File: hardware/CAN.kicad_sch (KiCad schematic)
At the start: 7 parts, among them U4 MCP2542FDxMF

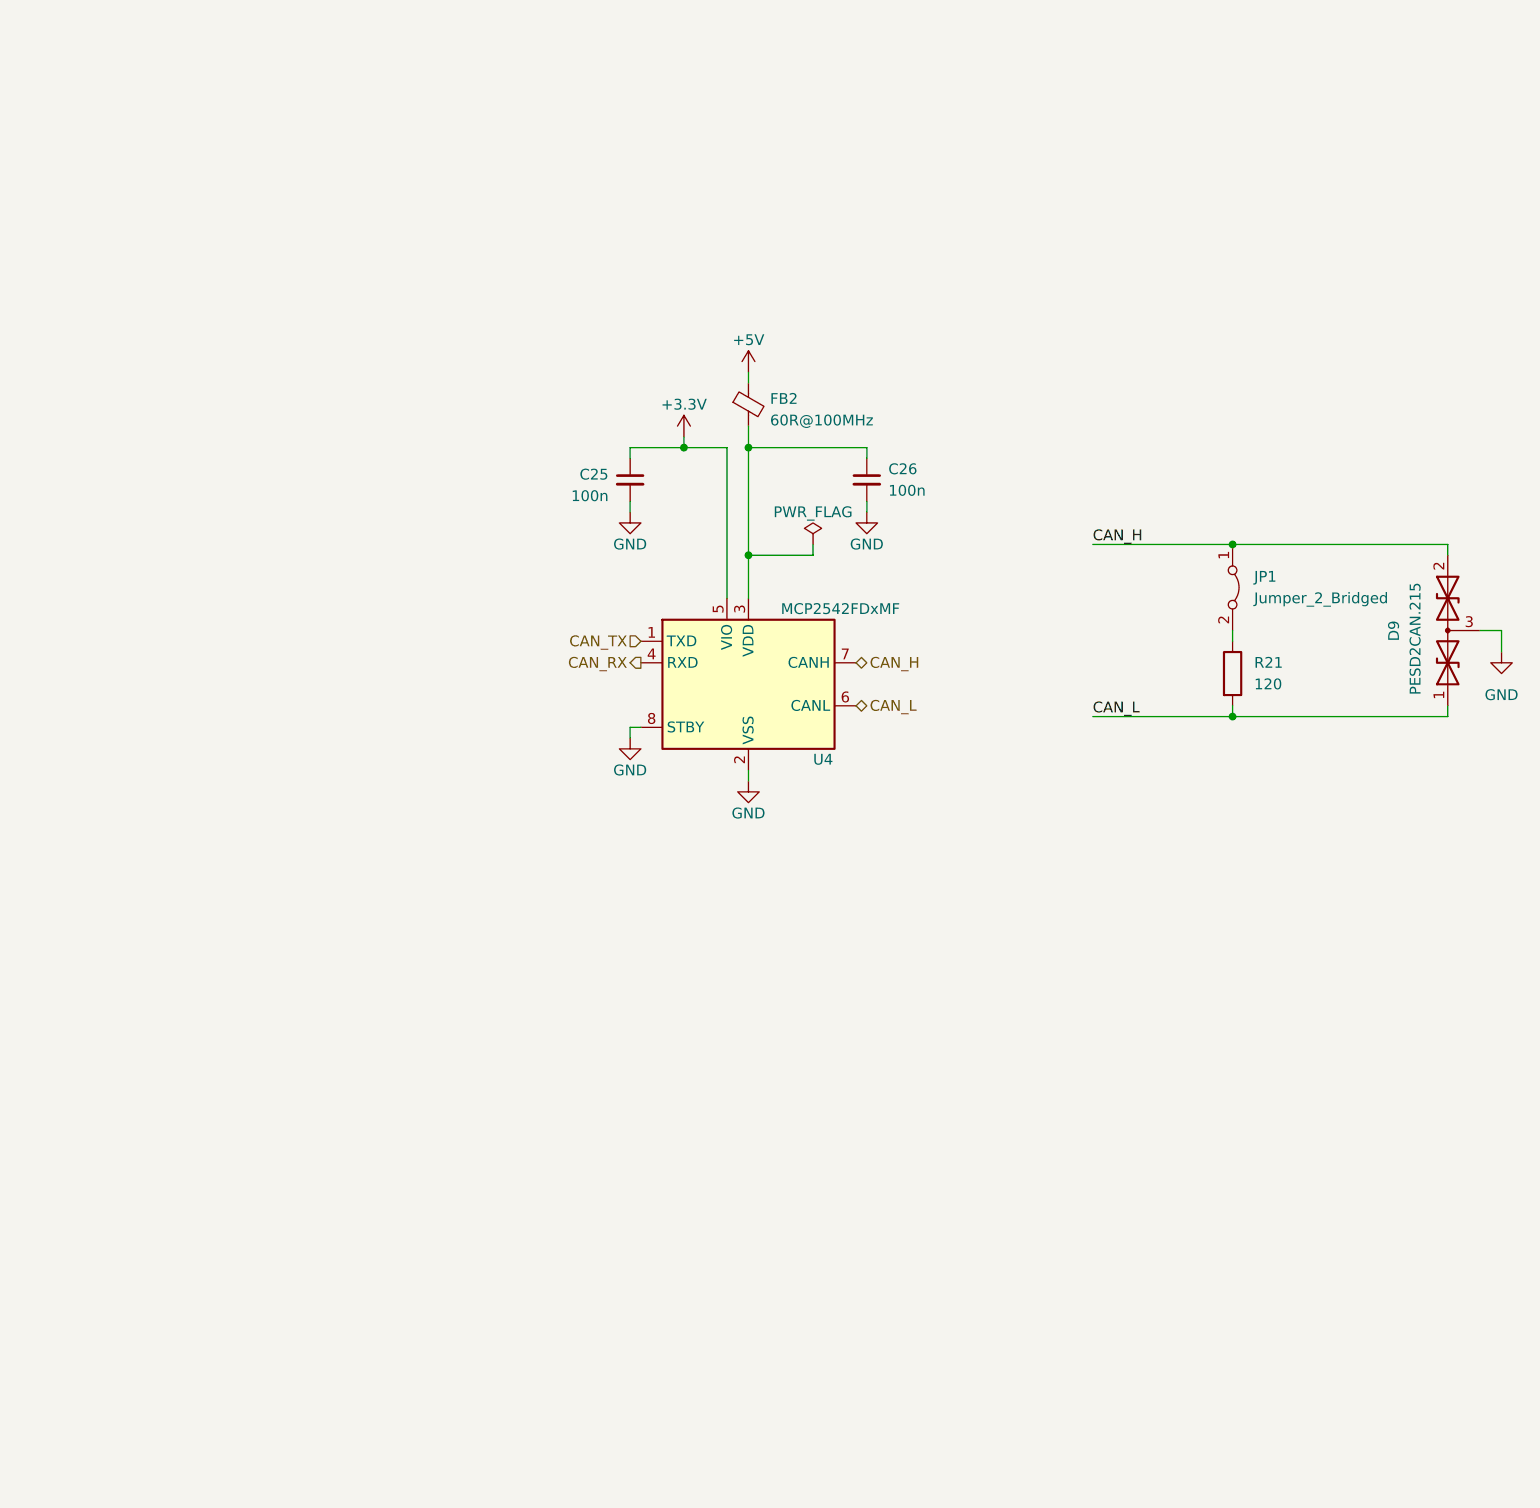
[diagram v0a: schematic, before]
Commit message: Changed CAN to isolated and added a new board-to-board plug
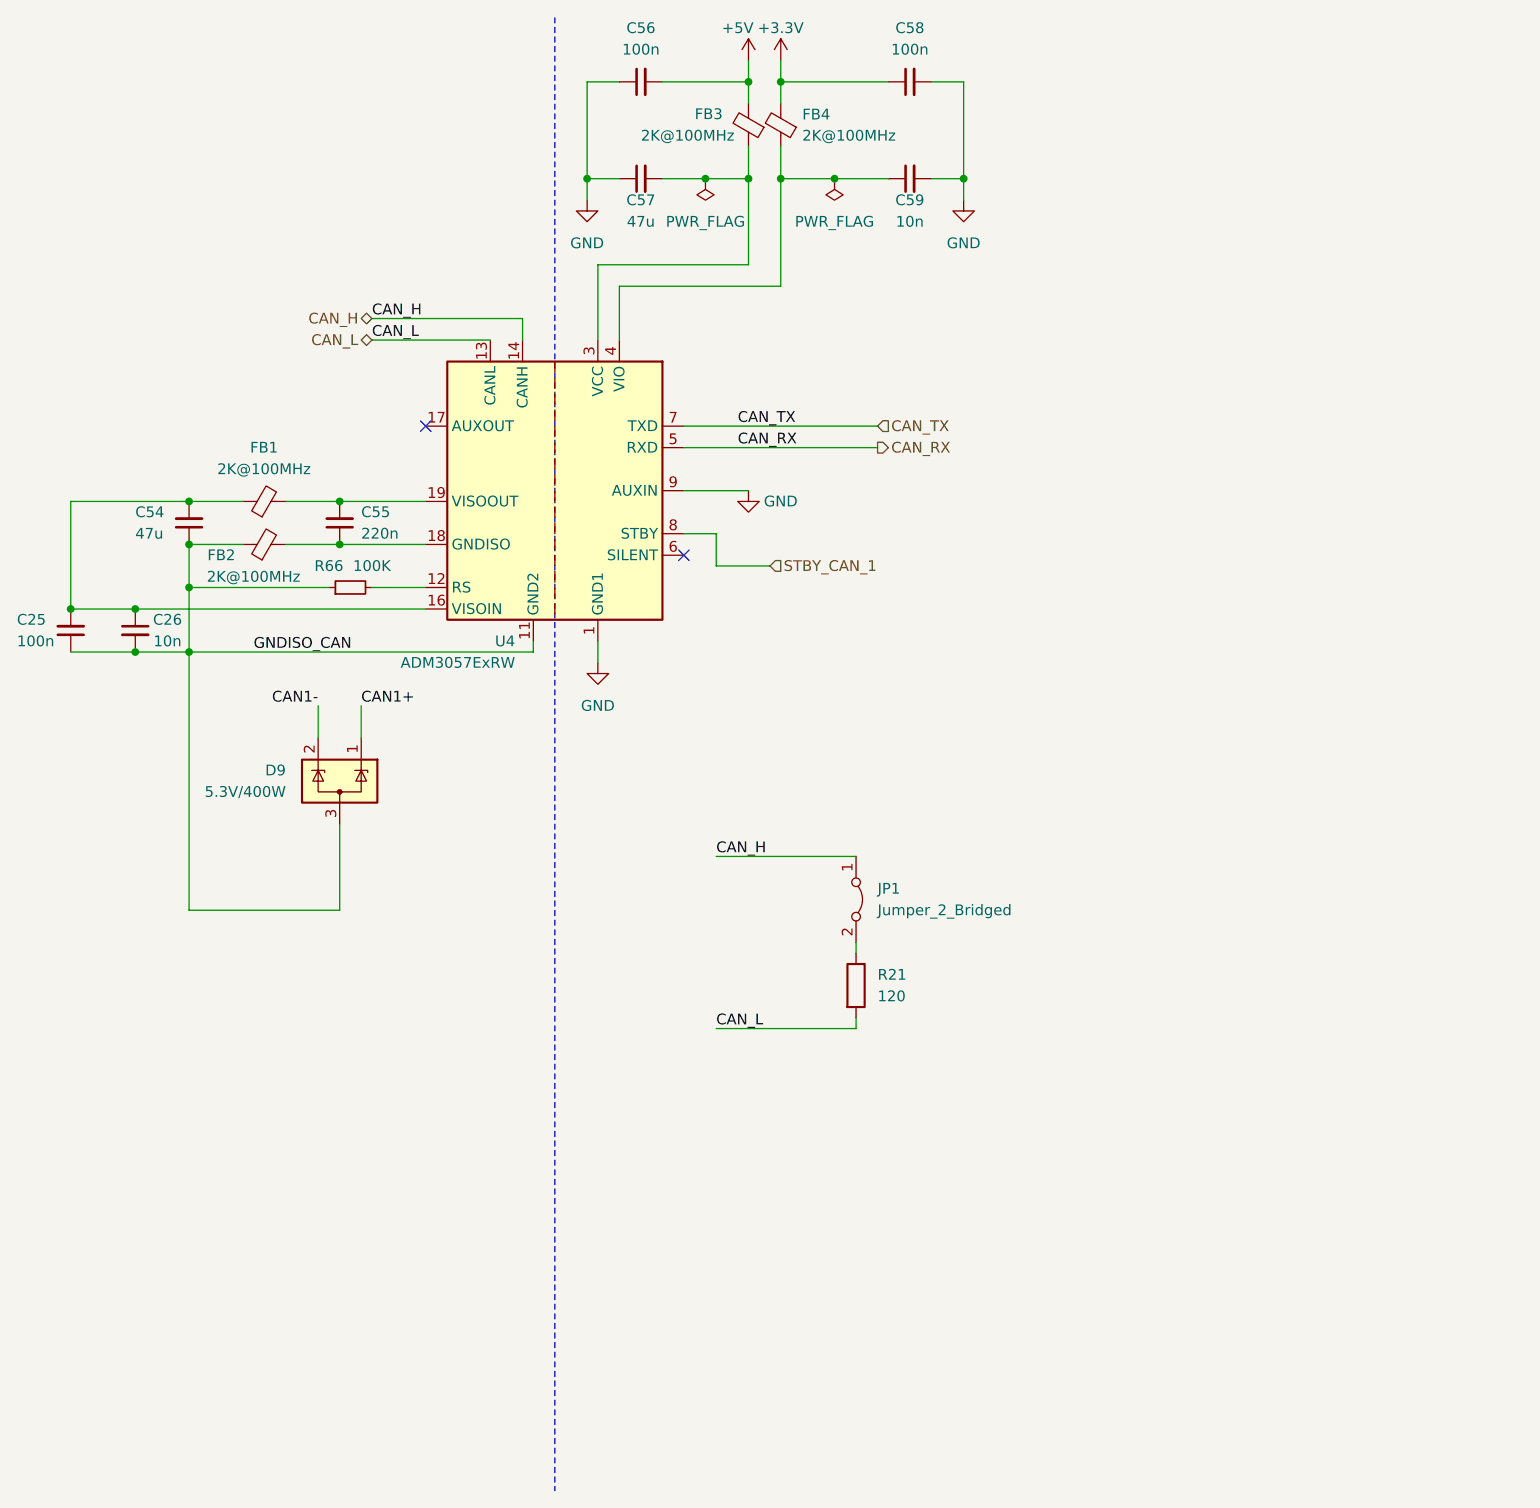
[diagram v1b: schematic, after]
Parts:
- removed D9: PESD2CAN.215, Package_TO_SOT_SMD:SOT-23, symbol BMS_LV_2022-rescue:D_TVS_x2_AAC-Device
- removed U4: MCP2542FDxMF, Package_DFN_QFN:DFN-8-1EP_3x3mm_P0.65mm_EP1.55x2.4mm, symbol Interface_CAN_LIN:MCP2542FDxMF
- added C54, C57: 47u, Capacitor_SMD:C_0603_1608Metric_Pad1.08x0.95mm_HandSolder, symbol Device:C_Small
- added C55: 220n, Capacitor_SMD:C_0603_1608Metric_Pad1.08x0.95mm_HandSolder, symbol Device:C_Small
- added C56, C58: 100n, Capacitor_SMD:C_0603_1608Metric_Pad1.08x0.95mm_HandSolder, symbol Device:C_Small
- added C59: 10n, Capacitor_SMD:C_0603_1608Metric_Pad1.08x0.95mm_HandSolder, symbol Device:C_Small
- added D9: 5.3V/400W, Package_TO_SOT_SMD:SOT-23-3, symbol Power_Protection:ESDA5V3L
- added FB1, FB3, FB4: 2K@100MHz, Inductor_SMD:L_0805_2012Metric_Pad1.05x1.20mm_HandSolder, symbol Device:FerriteBead_Small
- added R66: 100K, Resistor_SMD:R_0603_1608Metric_Pad0.98x0.95mm_HandSolder, symbol Device:R_Small
- added U4: ADM3057ExRW, Package_SO:SOIC-20W_7.5x12.8mm_P1.27mm, symbol Interface_CAN_LIN:ADM3057ExRW
- C26: value 100n -> 10n
- FB2: value 60R@100MHz -> 2K@100MHz; footprint Inductor_SMD:L_0603_1608Metric -> Inductor_SMD:L_0805_2012Metric_Pad1.05x1.20mm_HandSolder
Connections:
- net +3.3V: now also C58.1, FB4.2; no longer C25.1
- net +5V: now also C56.2, FB3.2; no longer FB2.1
- net CAN_H: now also U4.14 (CANH)
- net CAN_L: now also U4.13 (CANL)
- net CAN_RX: now also U4.5 (RXD)
- net CAN_TX: now also U4.7 (TXD)
- net GND: now also C56.1, C57.1, C58.2, C59.2, U4.1 (GND1), U4.10 (GND1), U4.2 (GND1), U4.9 (AUXIN); no longer C25.2, C26.2
- net at FB2.2: now also C55.1, U4.18 (GNDISO), U4.20 (GNDISO); no longer C26.1
- new net: C57.2, FB3.1, U4.3 (VCC)
- new net: R66.2, U4.12 (RS)
- new net: C25.2, C26.1, C54.2, FB1.1, U4.16 (VISOIN)
- new net: C55.2, FB1.2, U4.19 (VISOOUT)
- new net: C59.1, FB4.1, U4.4 (VIO)
- new net CAN1+: D9.1 (K)
- new net CAN1-: D9.2 (K)
- new net GNDISO_CAN: C25.1, C26.2, C54.1, D9.3 (A), FB2.1, R66.1, U4.11 (GND2), U4.15 (GND2)
- new net STBY_CAN_1: U4.8 (STBY)
- no-connect marks 0 -> 2
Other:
- moved on the sheet: JP1, R21

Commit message: NEW SCHEMATIC
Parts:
- removed C54, C57: 47u, Capacitor_SMD:C_0603_1608Metric_Pad1.08x0.95mm_HandSolder, symbol Device:C_Small
- removed C55: 220n, Capacitor_SMD:C_0603_1608Metric_Pad1.08x0.95mm_HandSolder, symbol Device:C_Small
- removed C56, C58: 100n, Capacitor_SMD:C_0603_1608Metric_Pad1.08x0.95mm_HandSolder, symbol Device:C_Small
- removed C59: 10n, Capacitor_SMD:C_0603_1608Metric_Pad1.08x0.95mm_HandSolder, symbol Device:C_Small
- removed D9: 5.3V/400W, Package_TO_SOT_SMD:SOT-23-3, symbol Power_Protection:ESDA5V3L
- removed JP1: Jumper_2_Bridged, Connector_PinHeader_2.54mm:PinHeader_1x02_P2.54mm_Vertical, symbol Jumper:Jumper_2_Bridged
- removed R21: 120, Resistor_SMD:R_0603_1608Metric_Pad0.98x0.95mm_HandSolder, symbol Device:R
- removed R66: 100K, Resistor_SMD:R_0603_1608Metric_Pad0.98x0.95mm_HandSolder, symbol Device:R_Small
- added C20: 100n, Capacitor_SMD:C_0603_1608Metric_Pad1.08x0.95mm_HandSolder, symbol Device:C_Small
- added C21, C27: 10n, Capacitor_SMD:C_0603_1608Metric_Pad1.08x0.95mm_HandSolder, symbol Device:C_Small
- added C22, C23, C24: 47u, Capacitor_SMD:C_0805_2012Metric_Pad1.18x1.45mm_HandSolder, symbol Device:C_Small
- added R13: 100k, Resistor_SMD:R_0603_1608Metric_Pad0.98x0.95mm_HandSolder, symbol Device:R_Small
- C25: value 100n -> 47u; footprint Capacitor_SMD:C_0603_1608Metric_Pad1.08x0.95mm_HandSolder -> Capacitor_SMD:C_0805_2012Metric_Pad1.18x1.45mm_HandSolder; Done? (none) -> y; Mouser Part Number (none) -> 81-GRM21BR60J476M01K; Mouser Price/Stock (none) -> https://www.mouser.pl/ProductDetail/Murata-Electronics/GRM2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
- C26: value 10n -> 100n; Done? (none) -> y; Mouser Part Number (none) -> 81-GCJ188R71H104KA2D; Mouser Price/Stock (none) -> https://www.mouser.pl/ProductDetail/Murata-Electronics/GCJ1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
- FB1, FB2, FB3, FB4: Done? (none) -> y; Mouser Part Number (none) -> 623-2508052027Y1; Mouser Price/Stock (none) -> https://www.mouser.pl/ProductDetail/Fair-Rite/2508052027Y1?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
- U4: Done? (none) -> y; Mouser Part Number (none) -> 584-ADM3057ETRWZ-EP; Mouser Price/Stock (none) -> https://www.mouser.pl/ProductDetail/Analog-Devices/ADM3057E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
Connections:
- net +5V: now also C24.2
- net GND: now also C25.2, C26.2, C24.1, C27.2
- net GNDISO: now reaches U4.18 (GNDISO), U4.20 (GNDISO)
- net GNDISO: now also FB2.1, C23.1; no longer FB2.2
- net VCC: now reaches FB3.1, U4.3 (VCC)
- net VCC: now also C25.1
- net RS: now reaches U4.12 (RS)
- net RS: now also R13.2
- net VISOIN: now reaches FB1.1, U4.16 (VISOIN)
- net VISOIN: now also C20.2, C21.1, C22.2; no longer C25.2, C26.1
- net VISOOUT: now reaches FB1.2, U4.19 (VISOOUT)
- net VISOOUT: now also C23.2
- net VIO: now reaches FB4.1, U4.4 (VIO)
- net VIO: now also C27.1
- net +3.3V renamed +3V3
- net +3V3: now also C26.1
- net CAN_H renamed CAN.P
- net CAN_L renamed CAN.N
- net CAN_RX renamed CAN.RX
- net CAN_TX renamed CAN.TX
- removed net GNDISO_CAN: C25.1, C26.2, FB2.1, U4.11 (GND2), U4.15 (GND2)
- net STBY_CAN_1 renamed STBY_CAN
- new net CAN_GND_ISO: C20.1, C21.2, C22.1, FB2.2, R13.1, U4.11 (GND2), U4.15 (GND2)
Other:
- note added: "1*"
- note added: "1* Slope control for 5 Mbps"
- note added: "CAN TRANSCEIVER"
- company: (none) -> Authors: Grzegorz Potocki Jędrzej Kasprzyk
- title: (none) -> PDUv3
